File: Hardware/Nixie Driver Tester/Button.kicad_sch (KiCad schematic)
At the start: 3 parts, among them SW1 SW_Omron_B3FS

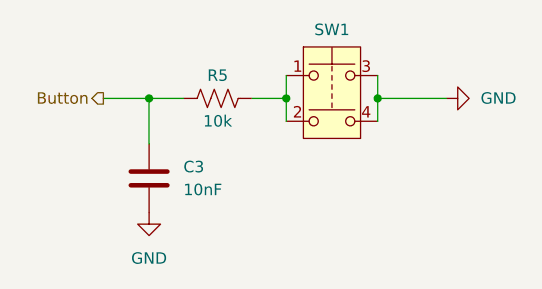
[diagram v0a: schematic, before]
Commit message: Initial component layout.
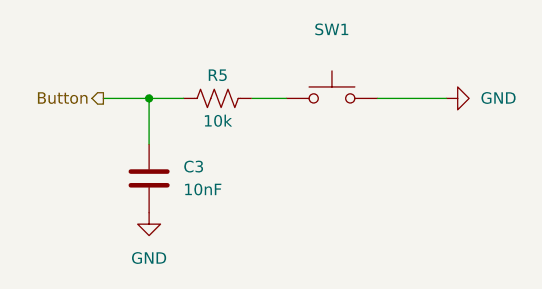
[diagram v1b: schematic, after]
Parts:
- R5: footprint Resistor_SMD:R_0201_0603Metric -> Resistor_SMD:R_0603_1608Metric
- SW1: symbol Swtich_:B3F-1000 -> Switch:SW_Push
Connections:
- net GND: now also SW1.2; no longer SW1.3, SW1.4
- net at R5.2, SW1.1: no longer SW1.2
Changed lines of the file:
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@@
 		(color 0 0 0 0)
 	)
-	(junction
-		(at 144.78 88.9)
-		(diameter 0)
-		(color 0 0 0 0)
-	)
-	(junction
-		(at 134.62 88.9)
-		(diameter 0)
-		(color 0 0 0 0)
-	)
 	(wire
 		(pts
@@
 		(pts
 			(xy 119.38 88.9) (xy 119.38 93.98)
-		)
-		(stroke
-			(width 0)
-			(type default)
-		)
-	)
-	(wire
-		(pts
-			(xy 144.78 88.9) (xy 144.78 91.44)
-		)
-		(stroke
-			(width 0)
-			(type default)
-		)
-	)
-	(wire
-		(pts
-			(xy 134.62 86.36) (xy 134.62 88.9)
-		)
-		(stroke
-			(width 0)
-			(type default)
-		)
-	)
-	(wire
-		(pts
-			(xy 134.62 88.9) (xy 134.62 91.44)
-		)
-		(stroke
-			(width 0)
-			(type default)
-		)
-	)
-	(wire
-		(pts
-			(xy 144.78 86.36) (xy 144.78 88.9)
 		)
 		(stroke
@@
 			)
 		)
-		(property "Footprint" "Resistor_SMD:R_0201_0603Metric"
+		(property "Footprint" "Resistor_SMD:R_0603_1608Metric"
 			(at 127.254 87.884 90)
 			(effects
@@
 	)
 	(symbol
-		(lib_id "Swtich_:B3F-1000")
+		(lib_id "Switch:SW_Push")
 		(at 139.7 88.9 0)
 		(unit 1)
@@
 		)
 		(property "Footprint" "Button_Switch_:B3F-10xx"
-			(at 139.7 81.28 0)
-			(effects
-				(font
-					(size 1.27 1.27)
-				)
-				(hide yes)
-			)
-		)
-		(property "Datasheet" "https://omronfs.omron.com/en_US/ecb/products/pdf/en-b3f.pdf"
+			(at 139.7 83.82 0)
+			(effects
+				(font
+					(size 1.27 1.27)
+				)
+				(hide yes)
+			)
+		)
+		(property "Datasheet" "~"
+			(at 139.7 83.82 0)
+			(effects
+				(font
+					(size 1.27 1.27)
+				)
+				(hide yes)
+			)
+		)
+		(property "Description" "Push button switch, generic, two pins"
 			(at 139.7 88.9 0)
 			(effects
@@
 			)
 		)
-		(property "Description" "Push button switch, 6x6mm four pins"
-			(at 139.7 88.9 0)
-			(effects
-				(font
-					(size 1.27 1.27)
-				)
-				(hide yes)
-			)
-		)
 		(pin "2"
 		)
 		(pin "1"
 		)
-		(pin "4"
-		)
-		(pin "3"
-		)
 		(instances
